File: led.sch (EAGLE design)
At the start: 12 parts

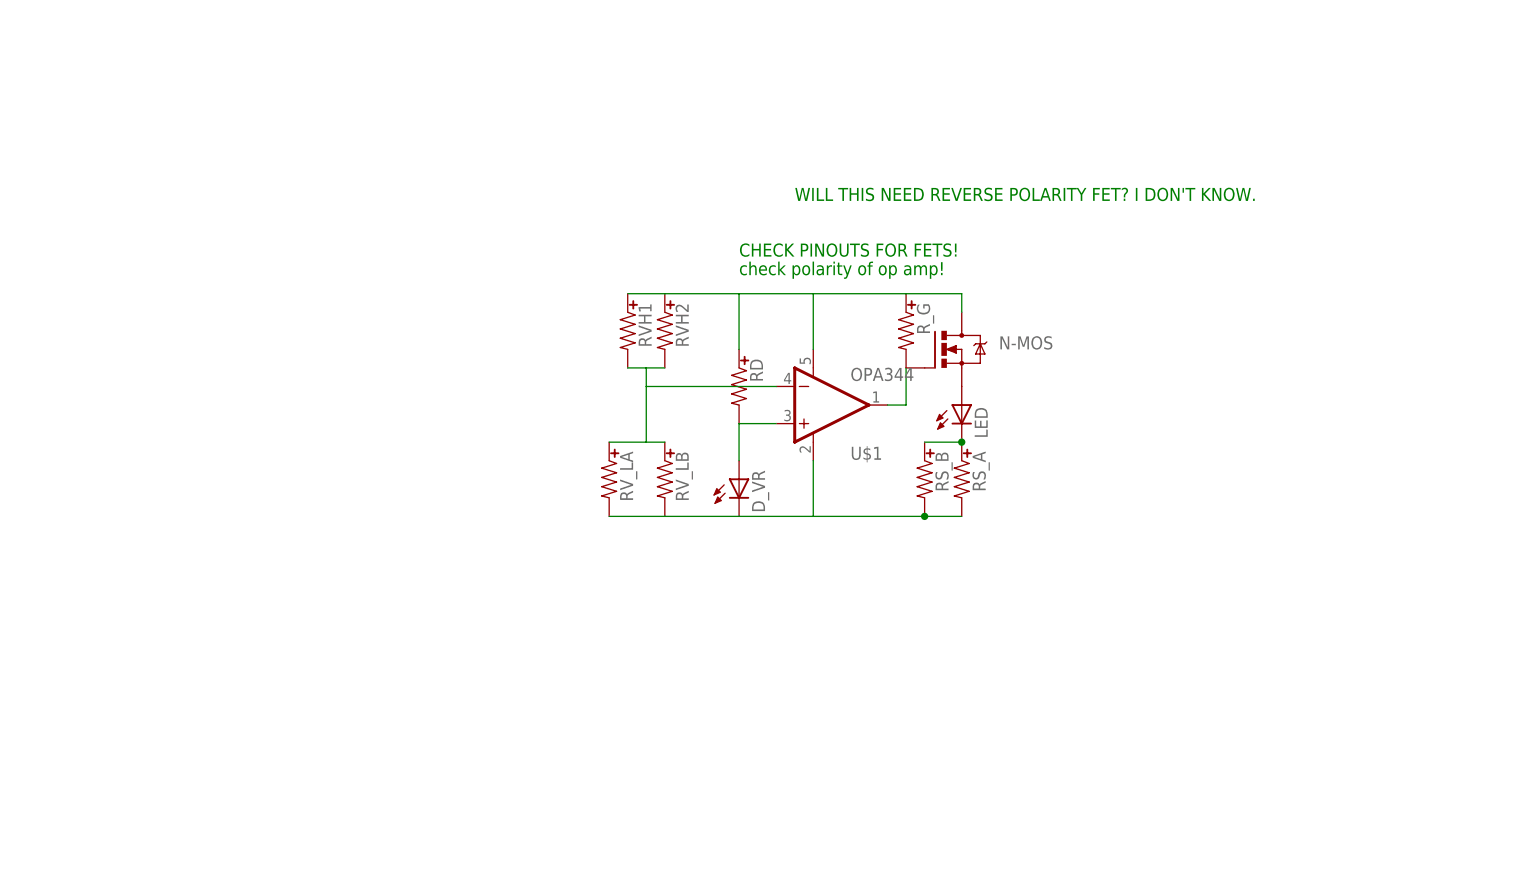
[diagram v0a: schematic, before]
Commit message: correct LED circuit
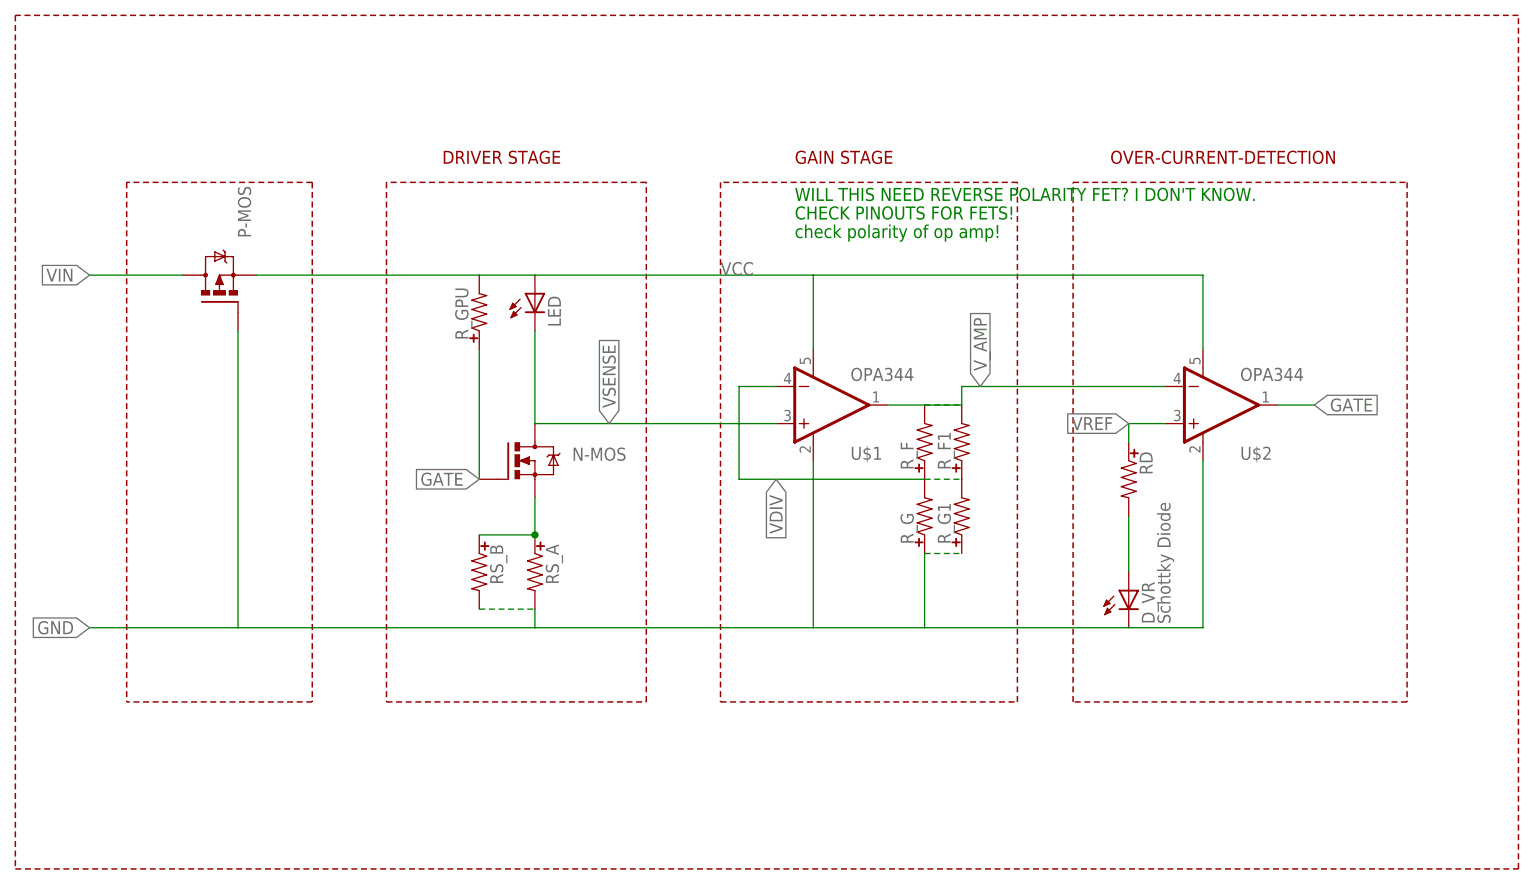
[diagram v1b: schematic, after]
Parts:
- removed RVH1, RVH2, RV_LA, RV_LB: (no value), tekdemo:RESISTORUNIVERSAL
- added P-MOS: MOSFET-PCHANNEL, tekdemo:MOSFET-PCHANNEL
- added R_F, R_F1, R_G1, R_GPU: (no value), tekdemo:RESISTORUNIVERSAL
- added U$2: OPA344, SparkFun-AnalogIC:OPA344
- D_VR: value (none) -> Schottky Diode
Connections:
- removed net LED+: LED.A, N-MOS.S
- removed net LED-: LED.C, RS_A.1, RS_B.1
- removed net N$7: RVH1.2, RVH2.2, RV_LA.1, RV_LB.1, U$1.-IN
- removed net N$8: D_VR.A, RD.2, U$1.+IN
- new net GATE: N-MOS.G, R_GPU.1, U$2.OUT
- new net N$2: N-MOS.S, RS_A.1, RS_B.1
- new net VCC: LED.A, P-MOS.S, R_GPU.2, U$1.V+, U$2.V+
- new net VDIV: R_F.1, R_F1.1, R_G.2, R_G1.2, U$1.-IN
- new net VREF: RD.1, U$2.+IN
- new net VSENSE: LED.C, N-MOS.D, U$1.+IN
- new net V_AMP: R_F.2, R_F1.2, U$1.OUT, U$2.-IN
- net GND: now also P-MOS.G, R_G.1, R_G1.1, U$2.V-; no longer RV_LA.2, RV_LB.2
- net N$3: now also D_VR.A, RD.2; no longer N-MOS.G, R_G.2, U$1.OUT
- net VIN: now also P-MOS.D; no longer N-MOS.D, RD.1, RVH1.1, RVH2.1, R_G.1, U$1.V+
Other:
- note added: "DRIVER STAGE"
- note added: "GAIN STAGE"
- note added: "OVER-CURRENT-DETECTION"
- moved on the sheet: D_VR, LED, N-MOS, RD, RS_A, RS_B, R_G

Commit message: routed led board
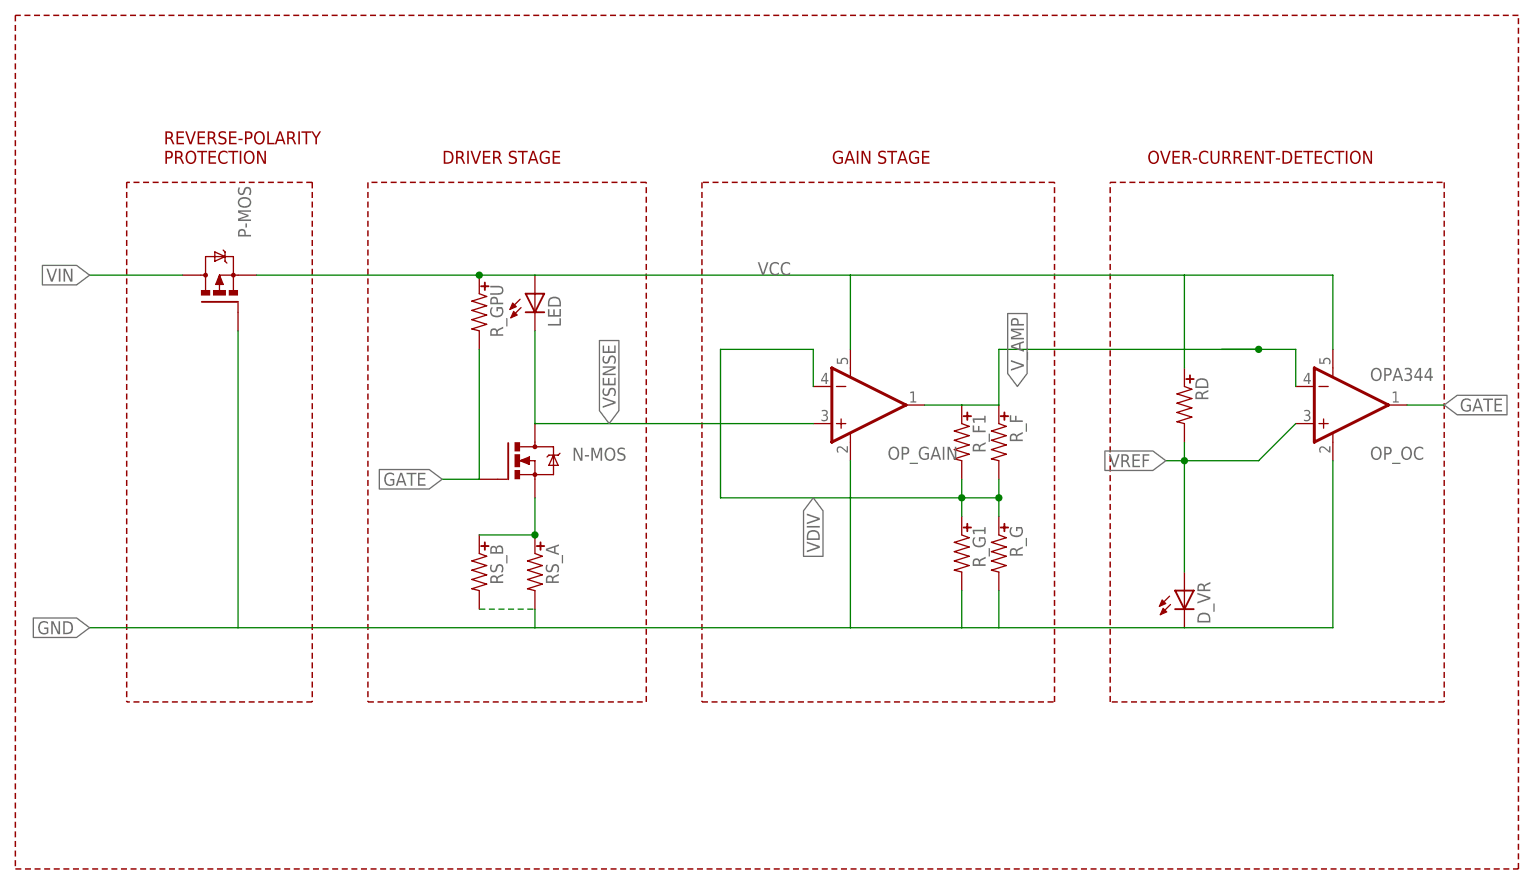
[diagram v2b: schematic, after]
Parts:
- removed U$1, U$2: OPA344, SparkFun-AnalogIC:OPA344
- added OP_GAIN, OP_OC: OPA344, SparkFun-AnalogIC:OPA344
- D_VR: value Schottky Diode -> (none)
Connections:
- removed net N$3: D_VR.A, RD.2
- net GATE: now also OP_OC.OUT, R_GPU.2; no longer R_GPU.1, U$2.OUT
- net GND: now also OP_GAIN.V-, OP_OC.V-, R_G.2, R_G1.2; no longer R_G.1, R_G1.1, U$1.V-, U$2.V-
- net VCC: now also OP_GAIN.V+, OP_OC.V+, RD.1, R_GPU.1; no longer R_GPU.2, U$1.V+, U$2.V+
- net VDIV: now also OP_GAIN.-IN, R_F.2, R_F1.2, R_G.1, R_G1.1; no longer R_F.1, R_F1.1, R_G.2, R_G1.2, U$1.-IN
- net VREF: now also D_VR.A, OP_OC.+IN, RD.2; no longer RD.1, U$2.+IN
- net VSENSE: now also OP_GAIN.+IN; no longer U$1.+IN
- net V_AMP: now also OP_GAIN.OUT, OP_OC.-IN, R_F.1, R_F1.1; no longer R_F.2, R_F1.2, U$1.OUT, U$2.-IN
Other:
- note added: "REVERSE-POLARITY PROTECTION"
- note removed: "CHECK PINOUTS FOR FETS!"
- note removed: "WILL THIS NEED REVERSE POLARITY FET? I DON'T KNOW."
- note removed: "check polarity of op amp!"
- moved on the sheet: D_VR, RD, R_F, R_F1, R_G, R_G1, R_GPU
